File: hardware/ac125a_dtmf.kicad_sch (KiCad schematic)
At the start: 12 parts

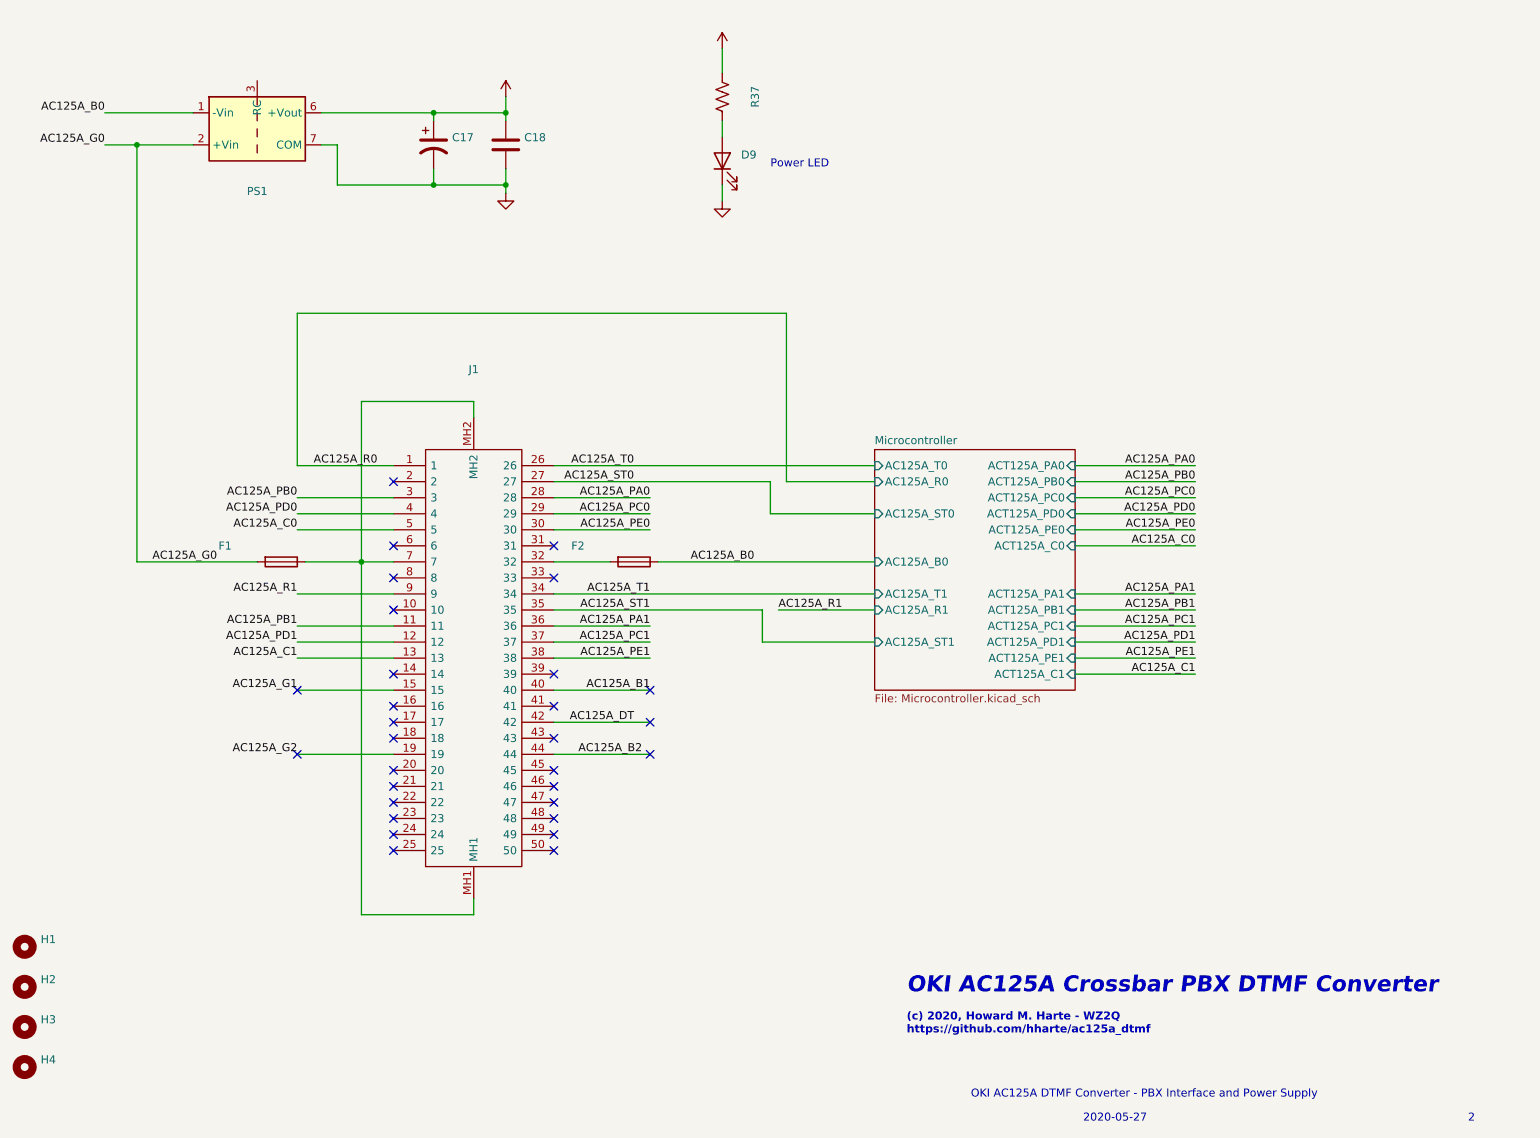
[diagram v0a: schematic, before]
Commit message: Fix a couple DRC errors in the layout.
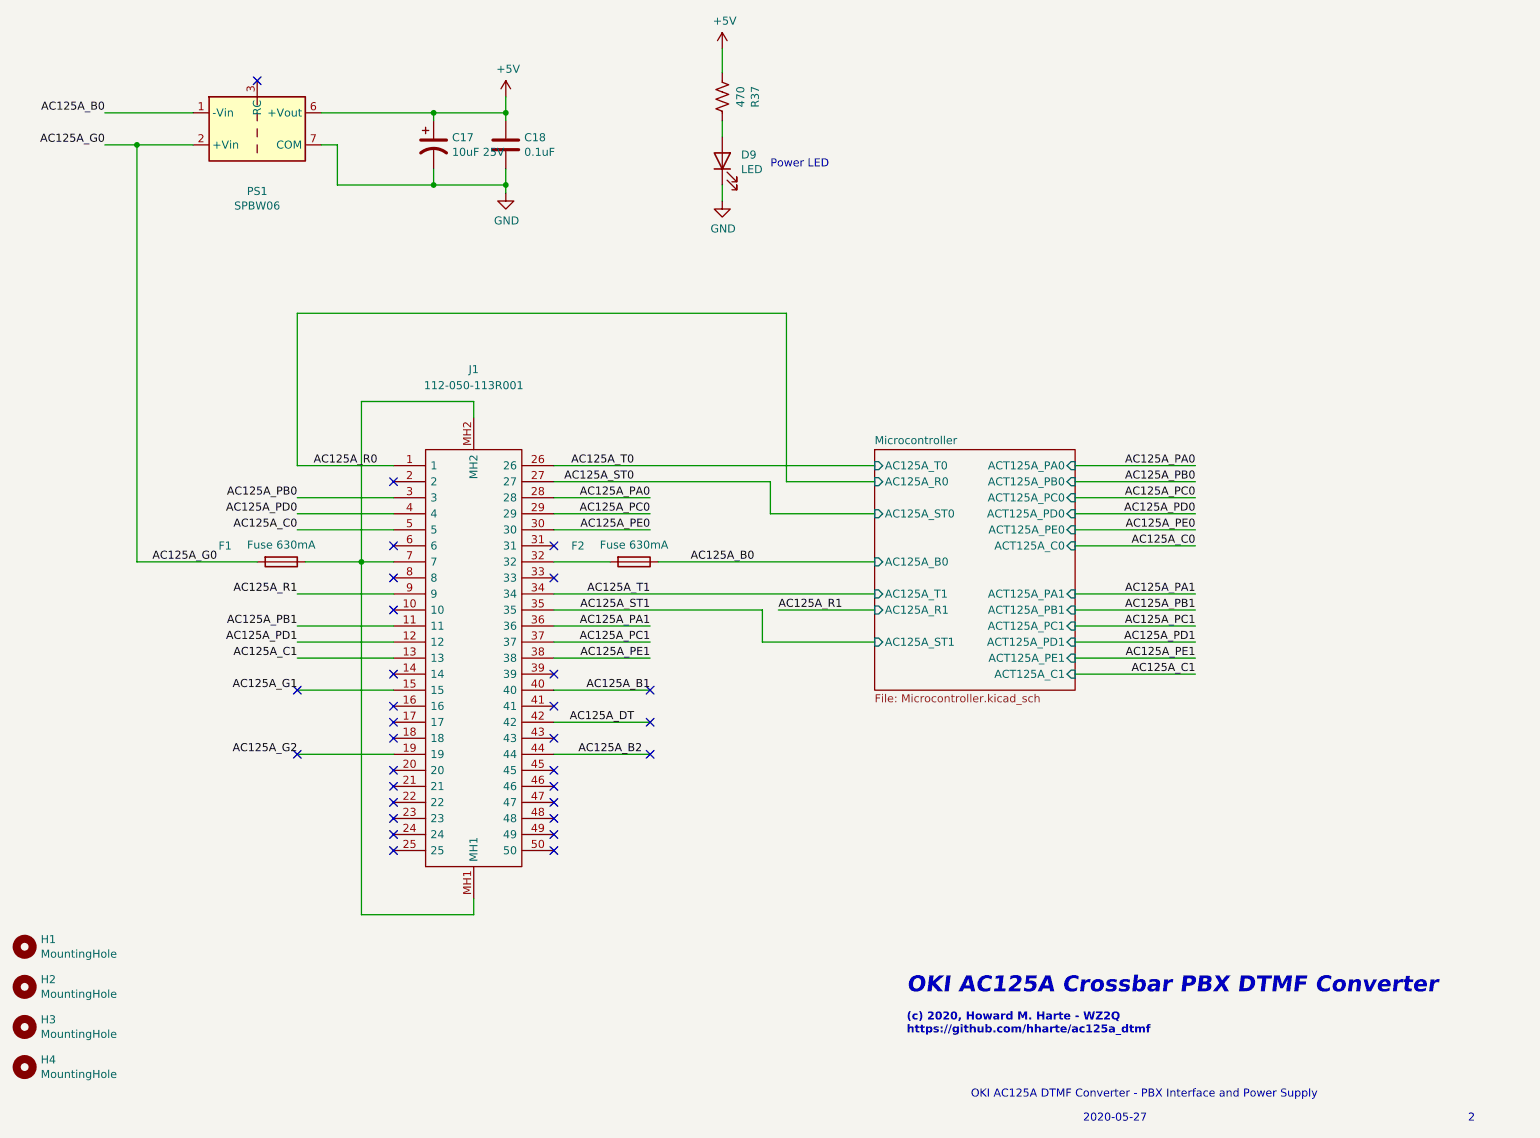
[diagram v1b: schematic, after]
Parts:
- C17: value (none) -> 10uF 25V; footprint (none) -> Capacitor_THT:CP_Radial_D6.3mm_P2.50mm
- C18: value (none) -> 0.1uF; footprint (none) -> Capacitor_THT:C_Disc_D3.0mm_W2.0mm_P2.50mm
- D9: value (none) -> LED; footprint (none) -> LED_THT:LED_D5.0mm
- F1, F2: value (none) -> Fuse 630mA; footprint (none) -> Resistor_THT:R_Axial_DIN0309_L9.0mm_D3.2mm_P12.70mm_Horizontal
- H1, H2, H3, H4: value (none) -> MountingHole; footprint (none) -> MountingHole:MountingHole_3.7mm_Pad
- J1: value (none) -> 112-050-113R001; footprint (none) -> ac125a_dtmf:112050113R001
- PS1: value (none) -> SPBW06; footprint (none) -> Converter_DCDC:Converter_DCDC_TRACO_TMR-xxxx_THT
- R37: value (none) -> 470; footprint (none) -> Resistor_THT:R_Axial_DIN0207_L6.3mm_D2.5mm_P7.62mm_Horizontal
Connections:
- no-connect marks 30 -> 31
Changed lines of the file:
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@@
   (no_connect (at 124.46 123.19))
   (no_connect (at 99.06 148.59))
+  (no_connect (at 77.47 29.21))
   (no_connect (at 124.46 143.51))
   (no_connect (at 124.46 138.43))
@@
     (in_bom yes) (on_board yes)
     (property "Reference" "J1" (id 0) (at 111.76 74.93 90))
-    (property "Value" "" (id 1) (at 111.76 77.47 90))
-    (property "Footprint" "" (id 2) (at 104.14 86.36 0)
+    (property "Value" "112-050-113R001" (id 1) (at 111.76 77.47 90))
+    (property "Footprint" "ac125a_dtmf:112050113R001" (id 2) (at 104.14 86.36 0)
       (effects (font (size 1.27 1.27)) (justify left) hide)
     )
@@
   (symbol (lib_id "Device:R_US") (at 151.13 31.75 180) (unit 1)
     (in_bom yes) (on_board yes)
-    (property "Reference" "R?" (id 0) (at 156.337 31.75 90))
-    (property "Value" "" (id 1) (at 154.0256 31.75 90))
-    (property "Footprint" "" (id 2) (at 150.114 31.496 90)
+    (property "Reference" "R37" (id 0) (at 156.337 31.75 90))
+    (property "Value" "470" (id 1) (at 154.0256 31.75 90))
+    (property "Footprint" "Resistor_THT:R_Axial_DIN0207_L6.3mm_D2.5mm_P7.62mm_Horizontal" (id 2) (at 150.114 31.496 90)
       (effects (font (size 1.27 1.27)) hide)
     )
@@
   (symbol (lib_id "Device:LED") (at 151.13 41.91 90) (unit 1)
     (in_bom yes) (on_board yes)
-    (property "Reference" "D?" (id 0) (at 154.1018 40.9448 90)
-      (effects (font (size 1.27 1.27)) (justify right))
-    )
-    (property "Value" "" (id 1) (at 154.1018 43.2562 90)
-      (effects (font (size 1.27 1.27)) (justify right))
-    )
-    (property "Footprint" "" (id 2) (at 151.13 41.91 0)
+    (property "Reference" "D9" (id 0) (at 154.1018 40.9448 90)
+      (effects (font (size 1.27 1.27)) (justify right))
+    )
+    (property "Value" "LED" (id 1) (at 154.1018 43.2562 90)
+      (effects (font (size 1.27 1.27)) (justify right))
+    )
+    (property "Footprint" "LED_THT:LED_D5.0mm" (id 2) (at 151.13 41.91 0)
       (effects (font (size 1.27 1.27)) hide)
     )
@@
   (symbol (lib_id "power:+5V") (at 151.13 24.13 0) (unit 1)
     (in_bom yes) (on_board yes)
-    (property "Reference" "#PWR?" (id 0) (at 151.13 27.94 0)
-      (effects (font (size 1.27 1.27)) hide)
-    )
-    (property "Value" "" (id 1) (at 151.511 19.7358 0))
+    (property "Reference" "#PWR0108" (id 0) (at 151.13 27.94 0)
+      (effects (font (size 1.27 1.27)) hide)
+    )
+    (property "Value" "+5V" (id 1) (at 151.511 19.7358 0))
     (property "Footprint" "" (id 2) (at 151.13 24.13 0)
       (effects (font (size 1.27 1.27)) hide)
@@
       (effects (font (size 1.27 1.27)) hide)
     )
-    (property "Value" "" (id 1) (at 151.257 52.6542 0))
+    (property "Value" "GND" (id 1) (at 151.257 52.6542 0))
     (property "Footprint" "" (id 2) (at 151.13 48.26 0)
       (effects (font (size 1.27 1.27)) hide)
@@
     (in_bom yes) (on_board yes)
     (property "Reference" "F1" (id 0) (at 72.39 102.87 90))
-    (property "Value" "" (id 1) (at 81.28 102.7176 90))
-    (property "Footprint" "" (id 2) (at 81.28 103.632 90)
+    (property "Value" "Fuse 630mA" (id 1) (at 81.28 102.7176 90))
+    (property "Footprint" "Resistor_THT:R_Axial_DIN0309_L9.0mm_D3.2mm_P12.70mm_Horizontal" (id 2) (at 81.28 103.632 90)
       (effects (font (size 1.27 1.27)) hide)
     )
@@
     (in_bom yes) (on_board yes)
     (property "Reference" "F2" (id 0) (at 128.27 102.87 90))
-    (property "Value" "" (id 1) (at 137.16 102.7176 90))
-    (property "Footprint" "" (id 2) (at 137.16 103.632 90)
+    (property "Value" "Fuse 630mA" (id 1) (at 137.16 102.7176 90))
+    (property "Footprint" "Resistor_THT:R_Axial_DIN0309_L9.0mm_D3.2mm_P12.70mm_Horizontal" (id 2) (at 137.16 103.632 90)
       (effects (font (size 1.27 1.27)) hide)
     )
@@
       (effects (font (size 1.27 1.27)) (justify left))
     )
-    (property "Value" "" (id 1) (at 108.331 40.513 0)
-      (effects (font (size 1.27 1.27)) (justify left))
-    )
-    (property "Footprint" "" (id 2) (at 105.41 39.37 0)
+    (property "Value" "10uF 25V" (id 1) (at 108.331 40.513 0)
+      (effects (font (size 1.27 1.27)) (justify left))
+    )
+    (property "Footprint" "Capacitor_THT:CP_Radial_D6.3mm_P2.50mm" (id 2) (at 105.41 39.37 0)
       (effects (font (size 1.27 1.27)) hide)
     )
@@
     (in_bom yes) (on_board yes)
     (property "Reference" "PS1" (id 0) (at 77.47 46.7106 0))
-    (property "Value" "" (id 1) (at 77.47 49.022 0))
-    (property "Footprint" "" (id 2) (at 50.8 43.18 0)
+    (property "Value" "SPBW06" (id 1) (at 77.47 49.022 0))
+    (property "Footprint" "Converter_DCDC:Converter_DCDC_TRACO_TMR-xxxx_THT" (id 2) (at 50.8 43.18 0)
       (effects (font (size 1.27 1.27)) (justify left) hide)
     )
@@
       (effects (font (size 1.27 1.27)) hide)
     )
-    (property "Value" "" (id 1) (at 117.221 27.3558 0))
+    (property "Value" "+5V" (id 1) (at 117.221 27.3558 0))
     (property "Footprint" "" (id 2) (at 116.84 31.75 0)
       (effects (font (size 1.27 1.27)) hide)
@@
       (effects (font (size 1.27 1.27)) (justify left))
     )
-    (property "Value" "" (id 1) (at 119.761 40.513 0)
-      (effects (font (size 1.27 1.27)) (justify left))
-    )
-    (property "Footprint" "" (id 2) (at 117.8052 43.18 0)
+    (property "Value" "0.1uF" (id 1) (at 119.761 40.513 0)
+      (effects (font (size 1.27 1.27)) (justify left))
+    )
+    (property "Footprint" "Capacitor_THT:C_Disc_D3.0mm_W2.0mm_P2.50mm" (id 2) (at 117.8052 43.18 0)
       (effects (font (size 1.27 1.27)) hide)
     )
@@
       (effects (font (size 1.27 1.27)) hide)
     )
-    (property "Value" "" (id 1) (at 116.967 51.3842 0))
+    (property "Value" "GND" (id 1) (at 116.967 51.3842 0))
     (property "Footprint" "" (id 2) (at 116.84 46.99 0)
       (effects (font (size 1.27 1.27)) hide)
@@
       (effects (font (size 1.27 1.27)) (justify left))
     )
-    (property "Value" "" (id 1) (at 43.18 167.513 0)
-      (effects (font (size 1.27 1.27)) (justify left))
-    )
-    (property "Footprint" "" (id 2) (at 40.64 166.37 0)
+    (property "Value" "MountingHole" (id 1) (at 43.18 167.513 0)
+      (effects (font (size 1.27 1.27)) (justify left))
+    )
+    (property "Footprint" "MountingHole:MountingHole_3.7mm_Pad" (id 2) (at 40.64 166.37 0)
       (effects (font (size 1.27 1.27)) hide)
     )
@@
       (effects (font (size 1.27 1.27)) (justify left))
     )
-    (property "Value" "" (id 1) (at 43.18 173.863 0)
-      (effects (font (size 1.27 1.27)) (justify left))
-    )
-    (property "Footprint" "" (id 2) (at 40.64 172.72 0)
+    (property "Value" "MountingHole" (id 1) (at 43.18 173.863 0)
+      (effects (font (size 1.27 1.27)) (justify left))
+    )
+    (property "Footprint" "MountingHole:MountingHole_3.7mm_Pad" (id 2) (at 40.64 172.72 0)
       (effects (font (size 1.27 1.27)) hide)
     )
@@
       (effects (font (size 1.27 1.27)) (justify left))
     )
-    (property "Value" "" (id 1) (at 43.18 180.213 0)
-      (effects (font (size 1.27 1.27)) (justify left))
-    )
-    (property "Footprint" "" (id 2) (at 40.64 179.07 0)
+    (property "Value" "MountingHole" (id 1) (at 43.18 180.213 0)
+      (effects (font (size 1.27 1.27)) (justify left))
+    )
+    (property "Footprint" "MountingHole:MountingHole_3.7mm_Pad" (id 2) (at 40.64 179.07 0)
       (effects (font (size 1.27 1.27)) hide)
     )
@@
       (effects (font (size 1.27 1.27)) (justify left))
     )
-    (property "Value" "" (id 1) (at 43.18 186.563 0)
-      (effects (font (size 1.27 1.27)) (justify left))
-    )
-    (property "Footprint" "" (id 2) (at 40.64 185.42 0)
+    (property "Value" "MountingHole" (id 1) (at 43.18 186.563 0)
+      (effects (font (size 1.27 1.27)) (justify left))
+    )
+    (property "Footprint" "MountingHole:MountingHole_3.7mm_Pad" (id 2) (at 40.64 185.42 0)
       (effects (font (size 1.27 1.27)) hide)
     )
@@
     )
     (path "/00000000-0000-0000-0000-00005ecc0265"
-      (reference "J1") (unit 1) (value "112-050-113R001") (footprint "112050113R001")
+      (reference "J1") (unit 1) (value "112-050-113R001") (footprint "ac125a_dtmf:112050113R001")
     )
     (path "/00000000-0000-0000-0000-00005ebebadd/00000000-0000-0000-0000-00005ec2b556"
